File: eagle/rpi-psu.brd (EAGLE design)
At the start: 48.3 x 41.9 mm, 20 parts, among them IC1 LD117AV33, IC2 TINY85P, Q1 TIP125, T1 2N2222A

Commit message: Small tweaks
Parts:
- moved R2 3.82 mm to (36.8, 27.7)
- turned SW1 to 270 degrees
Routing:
- net RPI-USR: track 23.0 -> 34.2 mm
- net +3V3: track 76.5 -> 74.1 mm
- net N$1: track 5.39 -> 3.56 mm

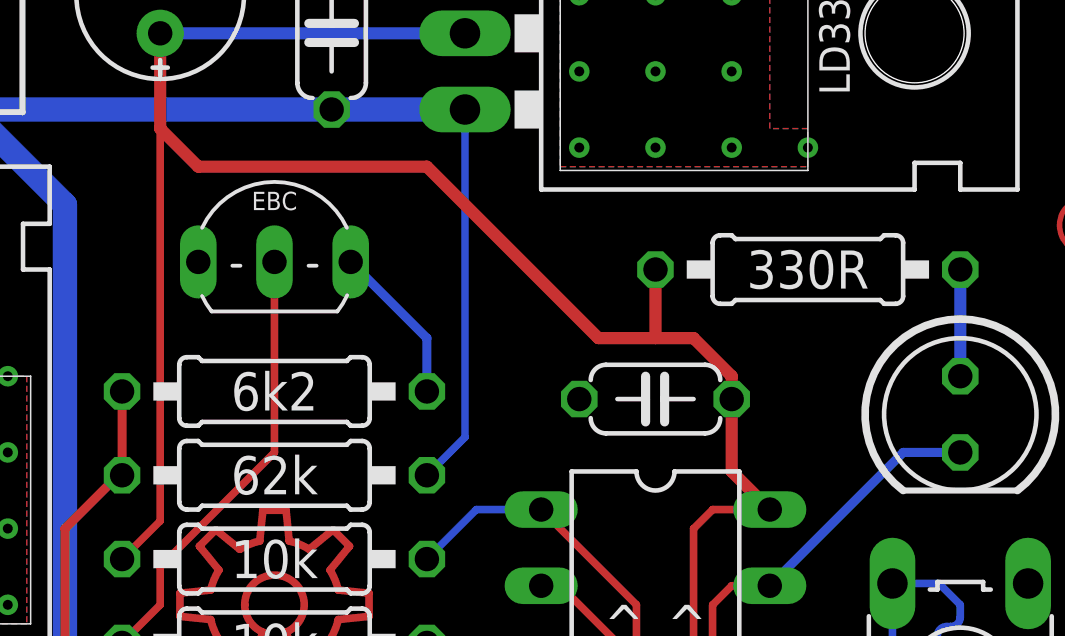
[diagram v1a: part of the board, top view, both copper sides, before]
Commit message: R2/R3 firmware updated, Replaced NPN transistor in R3 schematic
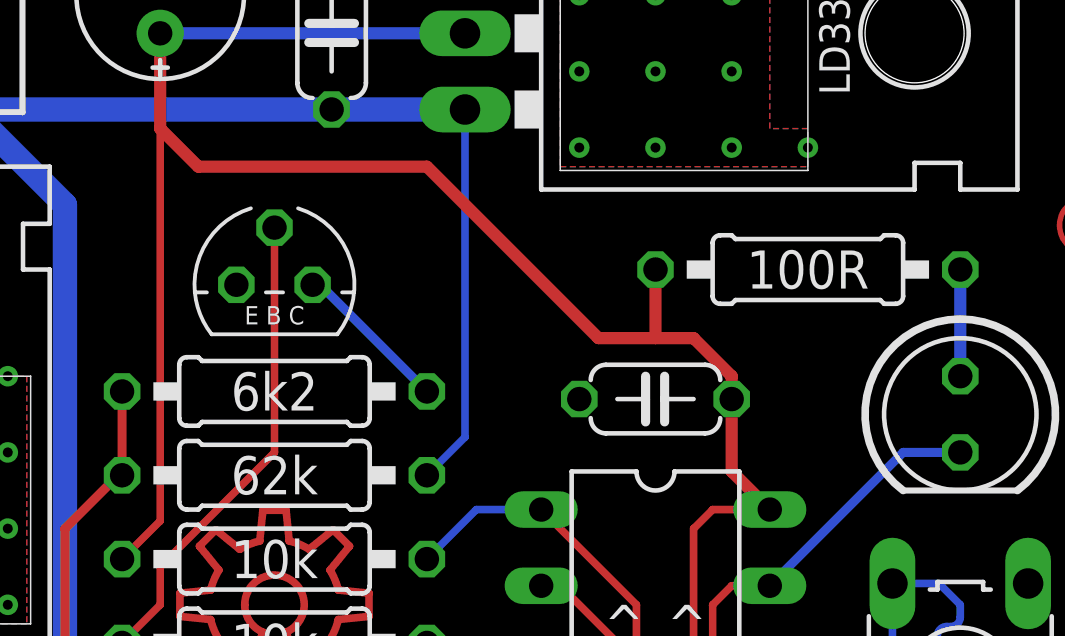
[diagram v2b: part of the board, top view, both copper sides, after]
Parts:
- R2: value 330R -> 100R
- T1: value 2N2222A -> P2N2222AG; device transistor:TO92-EBC -> transistor:TO92
- moved T1 2.03 mm to (19.1, 27.2)
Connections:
- net GND: now also T1.3; no longer T1.E
- net N$5: now also T1.2; no longer T1.B
- net N$6: now also T1.1; no longer T1.C
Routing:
- net N$5: track 17.6 -> 18.7 mm
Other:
- board text added: "E B C"
- board text removed: "EBC"
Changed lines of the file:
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@@
 <text x="6.35" y="24.765" size="1.016" layer="25" ratio="10" rot="R180" align="center">TIP125</text>
 <text x="37.719" y="35.56" size="1.016" layer="25" ratio="10" rot="R90" align="center">LD33V</text>
-<text x="19.05" y="29.972" size="0.6096" layer="21" ratio="20" align="center">EBC</text>
+<text x="19.05" y="26.162" size="0.6096" layer="21" ratio="20" align="center">E B C</text>
 </plain>
 <attributes>
@@
 </class>
 </classes>
-<designrules name="LaenPCBOrder *">
+<designrules name="LaenPCBOrder">
 <description language="de">&lt;b&gt;EAGLE Design Rules&lt;/b&gt;
 &lt;p&gt;
@@
 <param name="dpGapFactor" value="2.5"/>
 <param name="checkGrid" value="0"/>
-<param name="checkAngle" value="1"/>
+<param name="checkAngle" value="0"/>
 <param name="checkFont" value="1"/>
 <param name="checkRestrict" value="1"/>
@@
 <attribute name="VALUE" x="36.83" y="17.018" size="1.27" layer="27" ratio="10" rot="R270"/>
 </element>
-<element name="R2" library="resistor" package="0207/10" value="330R" x="36.83" y="27.686" smashed="yes">
+<element name="R2" library="resistor" package="0207/10" value="100R" x="36.83" y="27.686" smashed="yes">
 <attribute name="VALUE" x="36.83" y="27.686" size="1.27" layer="25" ratio="10" align="center"/>
 </element>
@@
 </element>
 <element name="Q1" library="transistor-power" package="TO220AH" value="TIP125" x="6.35" y="16.51" smashed="yes"/>
-<element name="T1" library="transistor" package="TO92-EBC" value="2N2222A" x="19.05" y="29.21" smashed="yes"/>
+<element name="T1" library="transistor" package="TO92" value="P2N2222AG" x="19.05" y="27.178" smashed="yes"/>
 <element name="R3" library="resistor" package="0207/10" value="240k" x="19.05" y="12.446" smashed="yes" rot="R180">
 <attribute name="VALUE" x="19.05" y="12.446" size="1.27" layer="25" ratio="10" rot="R180" align="center"/>
@@
 <contactref element="C3" pad="2"/>
 <contactref element="ICSP" pad="6"/>
-<contactref element="T1" pad="E"/>
+<contactref element="T1" pad="3"/>
 <contactref element="RPI" pad="6"/>
 <contactref element="RPI" pad="14"/>
@@
 </signal>
 <signal name="N$5">
-<contactref element="T1" pad="B"/>
+<contactref element="T1" pad="2"/>
 <contactref element="R3" pad="2"/>
 <wire x1="15.24" y1="17.78" x2="19.05" y2="21.59" width="0.254" layer="1"/>
-<wire x1="19.05" y1="21.59" x2="19.05" y2="27.94" width="0.254" layer="1"/>
+<wire x1="19.05" y1="21.59" x2="19.05" y2="29.083" width="0.254" layer="1"/>
 <contactref element="R4" pad="2"/>
 <wire x1="15.24" y1="17.78" x2="15.24" y2="16.51" width="0.254" layer="1"/>
@@
 <signal name="N$6">
 <contactref element="R5" pad="1"/>
-<contactref element="T1" pad="C"/>
-<wire x1="24.13" y1="23.622" x2="24.13" y2="25.4" width="0.3048" layer="16"/>
-<wire x1="24.13" y1="25.4" x2="21.59" y2="27.94" width="0.3048" layer="16"/>
+<contactref element="T1" pad="1"/>
+<wire x1="24.13" y1="23.622" x2="20.574" y2="27.178" width="0.3048" layer="16"/>
+<wire x1="20.574" y1="27.178" x2="20.32" y2="27.178" width="0.3048" layer="16"/>
 </signal>
 <signal name="HS2">

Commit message: Tweaks to R3 firmware and hardware silk
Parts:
- R4, R7: value 10k -> 1M
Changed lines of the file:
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@@
 <attribute name="VALUE" x="19.05" y="20.828" size="1.27" layer="25" ratio="10" align="center"/>
 </element>
-<element name="R7" library="resistor" package="0207/10" value="10k" x="19.05" y="9.652" smashed="yes" rot="R180">
+<element name="R7" library="resistor" package="0207/10" value="1M" x="19.05" y="9.652" smashed="yes" rot="R180">
 <attribute name="VALUE" x="19.05" y="9.652" size="1.27" layer="25" ratio="10" rot="R180" align="center"/>
 </element>
-<element name="R4" library="resistor" package="0207/10" value="10k" x="19.05" y="15.24" smashed="yes" rot="R180">
+<element name="R4" library="resistor" package="0207/10" value="1M" x="19.05" y="15.24" smashed="yes" rot="R180">
 <attribute name="VALUE" x="19.05" y="15.24" size="1.27" layer="25" ratio="10" rot="R180" align="center"/>
 </element>

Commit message: More silk tweaks. :)
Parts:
- R2: value 100R -> (none)
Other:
- board text added: "LED LIMIT"
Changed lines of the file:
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@@
 <layer number="17" name="Pads" color="2" fill="1" visible="yes" active="yes"/>
 <layer number="18" name="Vias" color="2" fill="1" visible="yes" active="yes"/>
-<layer number="19" name="Unrouted" color="6" fill="1" visible="yes" active="yes"/>
+<layer number="19" name="Unrouted" color="6" fill="1" visible="no" active="yes"/>
 <layer number="20" name="Dimension" color="15" fill="1" visible="yes" active="yes"/>
 <layer number="21" name="tPlace" color="7" fill="1" visible="yes" active="yes"/>
@@
 <layer number="25" name="tNames" color="7" fill="1" visible="yes" active="yes"/>
 <layer number="26" name="bNames" color="7" fill="1" visible="yes" active="yes"/>
-<layer number="27" name="tValues" color="7" fill="1" visible="no" active="yes"/>
-<layer number="28" name="bValues" color="7" fill="1" visible="no" active="yes"/>
+<layer number="27" name="tValues" color="7" fill="1" visible="yes" active="yes"/>
+<layer number="28" name="bValues" color="7" fill="1" visible="yes" active="yes"/>
 <layer number="29" name="tStop" color="7" fill="3" visible="no" active="yes"/>
 <layer number="30" name="bStop" color="7" fill="6" visible="no" active="yes"/>
 <layer number="31" name="tCream" color="7" fill="4" visible="no" active="yes"/>
 <layer number="32" name="bCream" color="7" fill="5" visible="no" active="yes"/>
-<layer number="33" name="tFinish" color="6" fill="3" visible="yes" active="yes"/>
-<layer number="34" name="bFinish" color="6" fill="6" visible="yes" active="yes"/>
+<layer number="33" name="tFinish" color="6" fill="3" visible="no" active="yes"/>
+<layer number="34" name="bFinish" color="6" fill="6" visible="no" active="yes"/>
 <layer number="35" name="tGlue" color="7" fill="4" visible="no" active="yes"/>
 <layer number="36" name="bGlue" color="7" fill="5" visible="no" active="yes"/>
-<layer number="37" name="tTest" color="7" fill="1" visible="yes" active="yes"/>
-<layer number="38" name="bTest" color="7" fill="1" visible="yes" active="yes"/>
-<layer number="39" name="tKeepout" color="4" fill="11" visible="yes" active="yes"/>
-<layer number="40" name="bKeepout" color="1" fill="11" visible="yes" active="yes"/>
-<layer number="41" name="tRestrict" color="4" fill="10" visible="yes" active="yes"/>
-<layer number="42" name="bRestrict" color="1" fill="10" visible="yes" active="yes"/>
-<layer number="43" name="vRestrict" color="2" fill="10" visible="yes" active="yes"/>
+<layer number="37" name="tTest" color="7" fill="1" visible="no" active="yes"/>
+<layer number="38" name="bTest" color="7" fill="1" visible="no" active="yes"/>
+<layer number="39" name="tKeepout" color="4" fill="11" visible="no" active="yes"/>
+<layer number="40" name="bKeepout" color="1" fill="11" visible="no" active="yes"/>
+<layer number="41" name="tRestrict" color="4" fill="10" visible="no" active="yes"/>
+<layer number="42" name="bRestrict" color="1" fill="10" visible="no" active="yes"/>
+<layer number="43" name="vRestrict" color="2" fill="10" visible="no" active="yes"/>
 <layer number="44" name="Drills" color="7" fill="1" visible="yes" active="yes"/>
 <layer number="45" name="Holes" color="7" fill="1" visible="yes" active="yes"/>
 <layer number="46" name="Milling" color="3" fill="1" visible="yes" active="yes"/>
 <layer number="47" name="Measures" color="7" fill="1" visible="yes" active="yes"/>
-<layer number="48" name="Document" color="7" fill="1" visible="no" active="yes"/>
+<layer number="48" name="Document" color="7" fill="1" visible="yes" active="yes"/>
 <layer number="49" name="Reference" color="7" fill="1" visible="yes" active="yes"/>
 <layer number="51" name="tDocu" color="7" fill="1" visible="yes" active="yes"/>
@@
 <text x="29.21" y="7.62" size="1.778" layer="25" font="vector" ratio="15" rot="R180" align="center">PSU</text>
 <text x="6.35" y="36.83" size="1.6764" layer="25" ratio="15" align="center">V5</text>
-<text x="31.75" y="15.875" size="1.27" layer="25" ratio="15" align="center">^_^</text>
+<text x="31.75" y="18.415" size="1.27" layer="25" ratio="15" align="center">^_^</text>
 <text x="6.35" y="24.765" size="1.016" layer="25" ratio="10" rot="R180" align="center">TIP125</text>
 <text x="37.719" y="35.56" size="1.016" layer="25" ratio="10" rot="R90" align="center">LD33V</text>
 <text x="19.05" y="26.162" size="0.6096" layer="21" ratio="20" align="center">E B C</text>
+<text x="36.83" y="27.686" size="0.6096" layer="25" font="vector" ratio="20" align="center">LED LIMIT</text>
 </plain>
 <attributes>
@@
 </autorouter>
 <elements>
-<element name="C1" library="resistor" package="C050-024X044" value="100nF" x="20.955" y="35.56" smashed="yes" rot="R90"/>
-<element name="C2" library="resistor" package="E2,5-6E" value="10µF" x="15.24" y="36.83" smashed="yes" rot="R90"/>
+<element name="C1" library="resistor" package="C050-024X044" value="100nF" x="20.955" y="35.56" smashed="yes" rot="R90">
+<attribute name="VALUE" x="21.082" y="39.878" size="0.8128" layer="27" font="vector" ratio="15" rot="R180" align="center"/>
+</element>
+<element name="C2" library="resistor" package="E2,5-6E" value="10µF" x="15.24" y="36.83" smashed="yes" rot="R90">
+<attribute name="VALUE" x="15.24" y="40.64" size="0.8128" layer="27" font="vector" ratio="15" rot="R180" align="center"/>
+</element>
 <element name="IC1" library="v-reg" package="TO220L1" value="LD117AV33" x="29.21" y="35.56" smashed="yes" rot="R270"/>
 <element name="J1" library="con-jack" package="DCJ0303" value="" x="6.35" y="36.83" smashed="yes" rot="R180">
@@
 <attribute name="VALUE" x="11.43" y="46.99" size="1.27" layer="27" rot="R270"/>
 </element>
-<element name="IC2" library="gamaral" package="DIL08" value="TINY85P" x="31.75" y="15.875" smashed="yes" rot="R270"/>
-<element name="C3" library="resistor" package="C050-024X044" value="100nF" x="31.75" y="23.368" smashed="yes" rot="R180"/>
+<element name="IC2" library="gamaral" package="DIL08" value="TINY85P" x="31.75" y="15.875" smashed="yes" rot="R270">
+<attribute name="VALUE" x="31.75" y="15.748" size="0.8128" layer="27" font="vector" ratio="15" align="center"/>
+</element>
+<element name="C3" library="resistor" package="C050-024X044" value="100nF" x="31.75" y="23.368" smashed="yes" rot="R180">
+<attribute name="VALUE" x="31.75" y="25.4" size="0.8128" layer="27" font="vector" ratio="15" rot="R180" align="center"/>
+</element>
 <element name="R1" library="resistor" package="0207/10" value="10k" x="19.05" y="18.034" smashed="yes">
 <attribute name="VALUE" x="19.05" y="18.034" size="1.27" layer="25" ratio="10" align="center"/>
@@
 <attribute name="VALUE" x="36.83" y="17.018" size="1.27" layer="27" ratio="10" rot="R270"/>
 </element>
-<element name="R2" library="resistor" package="0207/10" value="100R" x="36.83" y="27.686" smashed="yes">
+<element name="R2" library="resistor" package="0207/10" value="" x="36.83" y="27.686" smashed="yes">
 <attribute name="VALUE" x="36.83" y="27.686" size="1.27" layer="25" ratio="10" align="center"/>
 </element>

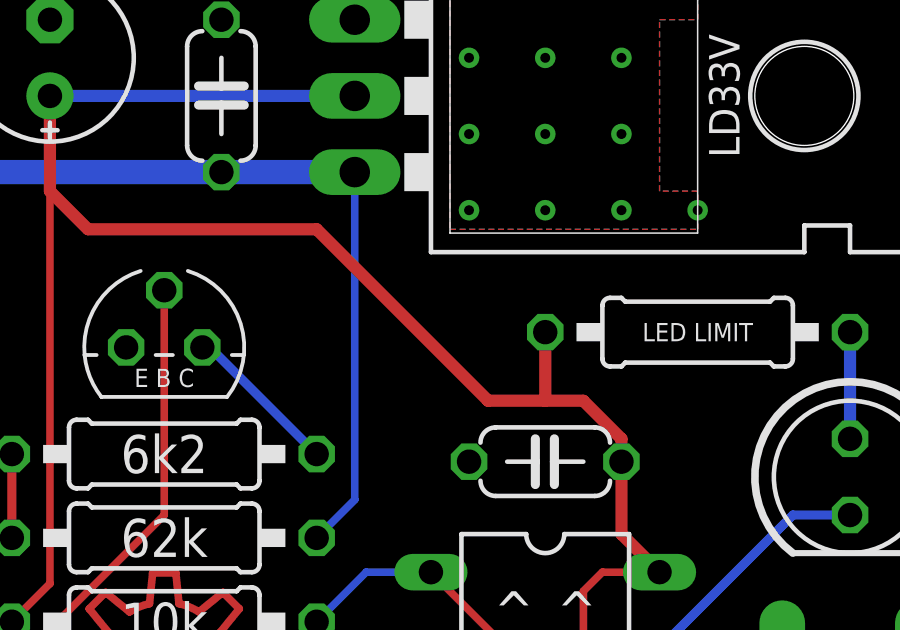
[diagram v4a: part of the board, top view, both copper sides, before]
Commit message: Small tweaks
Turned terminals back on for ground fills.

LED resistor trace moved.
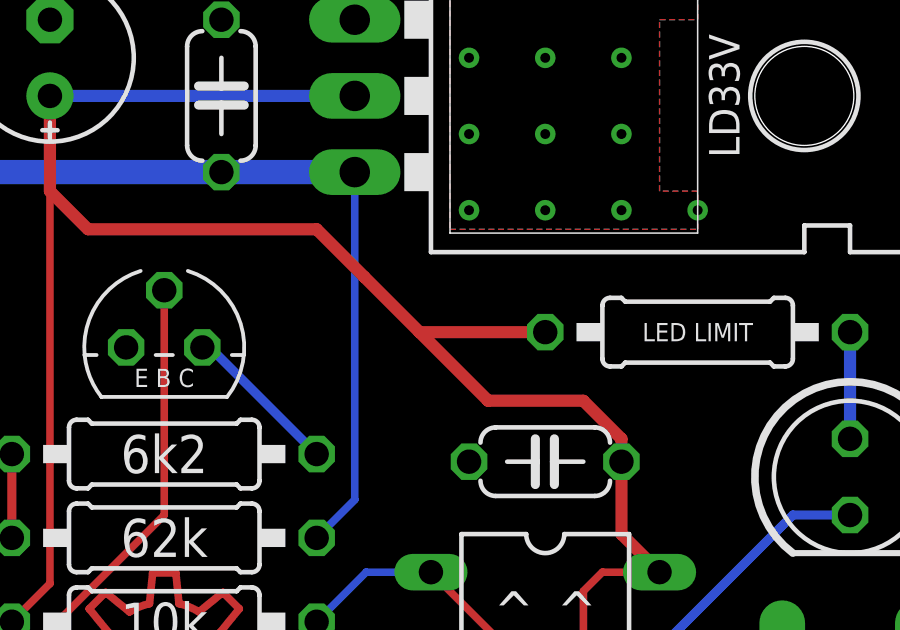
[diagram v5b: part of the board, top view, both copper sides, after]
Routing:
- net +3V3: track 74.1 -> 76.0 mm
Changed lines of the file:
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@@
 <layer number="17" name="Pads" color="2" fill="1" visible="yes" active="yes"/>
 <layer number="18" name="Vias" color="2" fill="1" visible="yes" active="yes"/>
-<layer number="19" name="Unrouted" color="6" fill="1" visible="no" active="yes"/>
+<layer number="19" name="Unrouted" color="6" fill="1" visible="yes" active="yes"/>
 <layer number="20" name="Dimension" color="15" fill="1" visible="yes" active="yes"/>
 <layer number="21" name="tPlace" color="7" fill="1" visible="yes" active="yes"/>
@@
 <layer number="46" name="Milling" color="3" fill="1" visible="yes" active="yes"/>
 <layer number="47" name="Measures" color="7" fill="1" visible="yes" active="yes"/>
-<layer number="48" name="Document" color="7" fill="1" visible="yes" active="yes"/>
+<layer number="48" name="Document" color="7" fill="1" visible="no" active="yes"/>
 <layer number="49" name="Reference" color="7" fill="1" visible="yes" active="yes"/>
 <layer number="51" name="tDocu" color="7" fill="1" visible="yes" active="yes"/>
@@
 <signals>
 <signal name="GND">
-<polygon width="0.4064" layer="1" isolate="0.4064" thermals="no" rank="2">
+<polygon width="0.4064" layer="1" isolate="0.4064" rank="2">
 <vertex x="0" y="41.91"/>
 <vertex x="48.26" y="41.91"/>
@@
 <contactref element="C2" pad="-"/>
 <contactref element="J1" pad="2"/>
-<polygon width="0.4064" layer="16" isolate="0.4064" thermals="no" rank="2">
+<polygon width="0.4064" layer="16" isolate="0.4064" rank="2">
 <vertex x="0" y="41.91"/>
 <vertex x="48.26" y="41.91"/>
@@
 <wire x1="34.29" y1="23.368" x2="34.29" y2="20.955" width="0.4064" layer="1"/>
 <wire x1="34.29" y1="20.955" x2="35.56" y2="19.685" width="0.4064" layer="1"/>
-<wire x1="29.845" y1="25.4" x2="24.13" y2="31.115" width="0.4064" layer="1"/>
+<wire x1="29.845" y1="25.4" x2="27.559" y2="27.686" width="0.4064" layer="1"/>
+<wire x1="25.7175" y1="29.5275" x2="24.13" y2="31.115" width="0.4064" layer="1"/>
 <wire x1="34.29" y1="23.368" x2="34.29" y2="24.13" width="0.4064" layer="1"/>
 <wire x1="34.29" y1="24.13" x2="33.02" y2="25.4" width="0.4064" layer="1"/>
-<wire x1="33.02" y1="25.4" x2="31.75" y2="25.4" width="0.4064" layer="1"/>
-<wire x1="31.75" y1="25.4" x2="29.845" y2="25.4" width="0.4064" layer="1"/>
-<wire x1="31.75" y1="27.686" x2="31.75" y2="25.4" width="0.4064" layer="1"/>
+<wire x1="33.02" y1="25.4" x2="29.845" y2="25.4" width="0.4064" layer="1"/>
+<wire x1="31.75" y1="27.686" x2="27.559" y2="27.686" width="0.4064" layer="1"/>
+<wire x1="27.559" y1="27.686" x2="25.7175" y2="29.5275" width="0.4064" layer="1"/>
 </signal>
 <signal name="RESET">
